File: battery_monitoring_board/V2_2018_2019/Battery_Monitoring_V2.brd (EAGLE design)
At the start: 57.2 x 127 mm, 88 parts, among them CON1 MOLEX_5566-2, CON2 SM03B-GHS-TB, CON3 SM03B-GHS-TB, J1 MKDS_5/2-6,352, J2 MKDS_5/2-6,352, J3 MKDS_5/2-6,352, J4 MKDS_5/2-6,352, J5 MKDS_5/2-6,352, J6 MKDS_5/2-6,352, J7 MKDS_5/2-6,352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

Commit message: Intermidiate Work-Board Tracing to be done
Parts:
- added D4: BZT52C10, Moira:SOD-123
- added J10, J11: MKDS_5/2-6,352, Moira:MKDS_5/2-6,35
- added Q15: PSMN1R5-30BLE, Moira:SOT404/D2PAK
- added Q16: TCLD1000CT, Moira:SOP-4L
- added Q8: SI7145DP, Si7145DP:SO-8/PPAK/TEST
- added R31, R32: 10k, adafruit:M1206
- added R33: 1k, adafruit:M1206
- added R34: 1k, adafruit:R0805
- added R35: 0.001Ohm, Moira:3920
- moved U$15 102.1 mm to (185.4, 10.2)
- moved U$18 17.8 mm to (116.8, 196.8)
- moved U$26 17.8 mm to (67.3, 196.8)
- moved U$24 16.5 mm to (116.8, 43.2)
- moved U$25 16.5 mm to (67.3, 43.2)
- moved JP5 10.2 mm to (85.1, 189.9)
- moved JP6 10.2 mm to (100.3, 189.9)
- moved R14 10.2 mm to (93.3, 189.9)
- moved R15 10.2 mm to (90.8, 189.9)
- moved C1 7.62 mm to (78.7, 175.3)
- moved C2 7.62 mm to (81.3, 165.1)
- moved CON2 7.62 mm to (116.4, 172.7)
- moved CON3 7.62 mm to (116.4, 172.7)
- moved U1 7.62 mm to (77.5, 179.1)
- moved U2 7.62 mm to (80.0, 168.9)
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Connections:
- new net +5V/2.6D: R34.1
- new net BATTERY5_IN: J10.2, Q8.S@1, Q8.S@2, Q8.S@3
- new net BATTERY_5: Q16.P$4, Q8.D@1, Q8.D@2, Q8.D@3, Q8.D@4, Q8.D@5, R35.P$2, U1.2
- new net MOTOR4: J11.1, R35.P$1, U1.1
- new net N$10: Q8.G, R31.2
- new net N$12: D4.P$2, J10.1, Q15.3S, R31.1, R32.1
- new net N$13: D4.P$1, Q15.1G, R32.2, R33.1
- new net N$15: Q16.P$3, R33.2
- new net N$16: Q16.P$1, R34.2
- net GND: now also J11.2, Q15.2D
- net MOTOR2: no longer U1.1
- net N$4: now also Q16.P$2
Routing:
- net VIN: track 34.9 -> 42.5 mm
- net POWER_BOARD: track 98.2 -> 105.8 mm
- net MOTOR1: track 135.4 -> 143.0 mm
- net ELECTRONICS_BATTERY: track 117.7 -> 125.4 mm
- net BATTERY_4: track 166.0 -> 173.6 mm
- net BATTERY_3: track 142.0 -> 149.7 mm
- net MOTOR3: track 100.8 -> 108.5 mm
- net BATTERY_2: track 120.4 -> 128.0 mm
- net +5V: track 26.2 -> 30.0 mm
- net SDA: track 77.8 -> 80.4 mm
- net SCL: track 66.8 -> 69.3 mm
- net +3V3: track 121.5 -> 123.9 mm
- net GND: track 2.05 -> 4.10 mm
- net MOTOR2: track 122.6 -> 121.2 mm
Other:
- board size 57.2 x 127 mm -> 57.2 x 161.3 mm

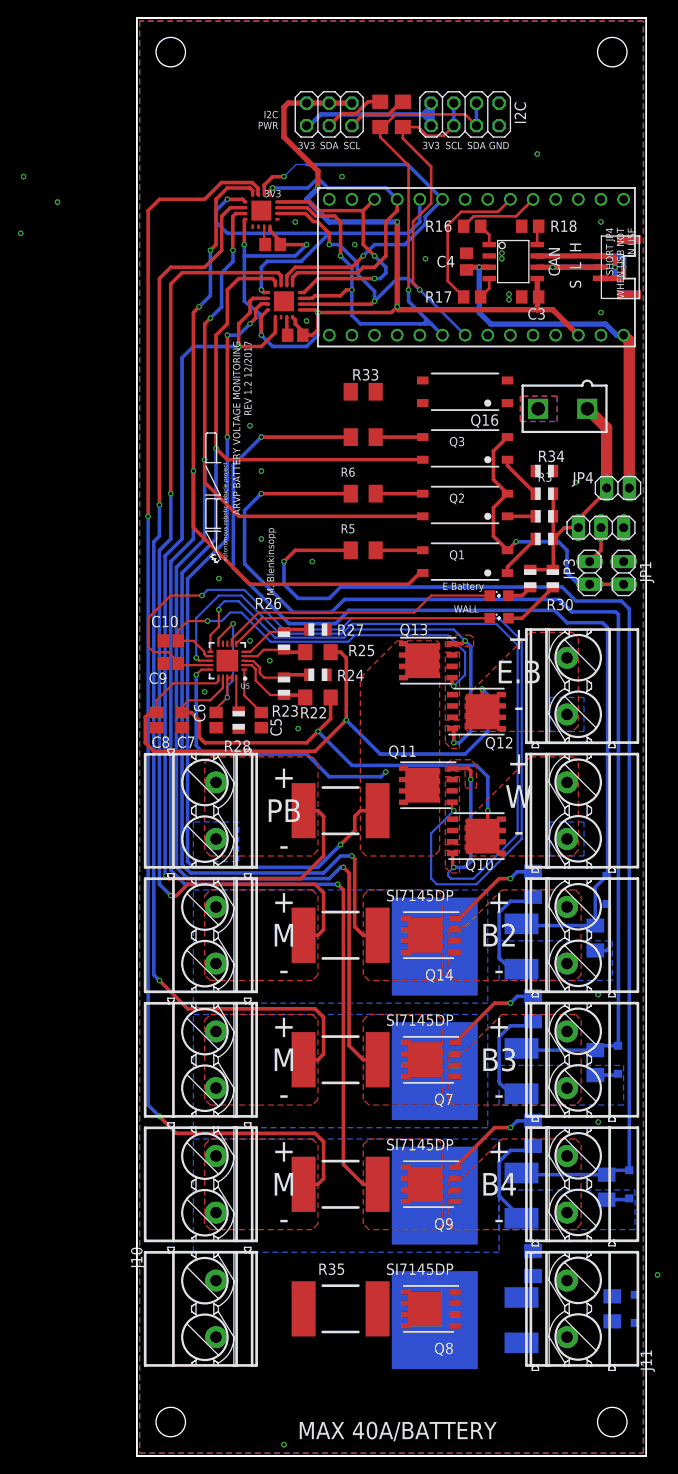
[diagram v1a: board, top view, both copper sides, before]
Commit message: Finished the Baterry Monitoring Board Layout and Schematic
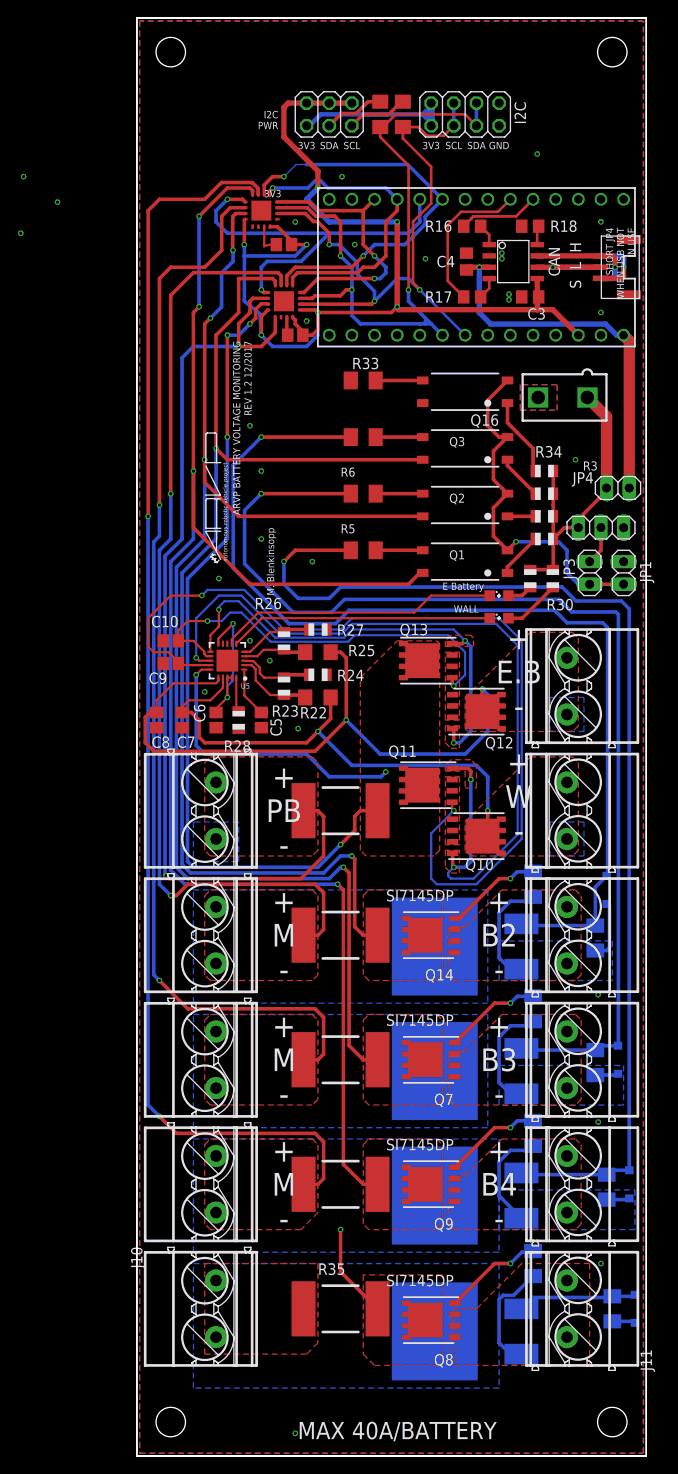
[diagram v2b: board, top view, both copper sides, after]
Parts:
- moved C1 1.27 mm to (80.0, 175.3)
- moved CON1 1.27 mm to (111.3, 158.1)
- moved R33 1.27 mm to (88.9, 160.0)
- moved Q8 1.27 mm to (96.5, 54.6)
- moved Q15 1.27 mm to (100.3, 53.3)
- turned R34 to 180 degrees
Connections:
- net N$12 renamed BATT5GND
- net N$13 renamed MG4
- removed net +5V/2.6D: R34.1
- net +5V: now also R34.1
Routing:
- net BATT5GND: track 0.00 -> 15.1 mm
- net MG4: track 0.00 -> 13.3 mm
- net N$10: track 0.00 -> 11.1 mm, vias 0 -> 1
- net BATTERY_5: track 0.00 -> 10.6 mm, vias 0 -> 1
- net N$16: track 0.00 -> 8.81 mm
- net N$4: track 32.2 -> 40.9 mm
- net N$15: track 0.00 -> 5.28 mm
- net +5V: track 30.0 -> 33.8 mm
- net GND: track 4.10 -> 5.70 mm
- net MOTOR3: track 108.5 -> 107.7 mm
- added copper zone on layer 1, net N$12
- added copper zone on layer 1, net N$13
- added copper zone on layer 1, net N$17
- added copper zone on layer 16, net N$18

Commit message: battery_monitoring_board: Fixed up a few mistakes
- Swapped battery terminal blocks around
- Changed polygon fill from hatch to solid
- Cleaned up polygons on 5th battery to match others
- Removed vestigial polygons on bottom layer
- Routed a few missing connections
- Added Mustafa's name
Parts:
- moved J10 39.4 mm to (111.8, 55.9), turned to 90 degrees
- moved J11 39.4 mm to (72.4, 55.9), turned to 270 degrees
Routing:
- net BATTERY_5: track 10.6 -> 146.4 mm, vias 1 -> 3
- net MOTOR4: track 0.00 -> 127.8 mm, vias 0 -> 2
- net MG4: track 13.3 -> 138.8 mm, vias 0 -> 2
- added copper zone on layer 16, net BATT5GND
- added copper zone on layer 1, net BATTERY5_IN
- added copper zone on layer 1, net BATTERY_5
- added copper zone on layer 1, net MOTOR4
- removed copper zone on layer 1, net N$12
- removed copper zone on layer 1, net N$13
- removed copper zone on layer 1, net N$17
- removed copper zone on layer 16, net N$18
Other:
- board text added: "M. Farow"
